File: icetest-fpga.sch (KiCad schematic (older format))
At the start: 25 parts

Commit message: add schematic notes
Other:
- note added: "CDONE pull up as per\nice40 handbook"
- note added: "RST high starts config process\nautomatically"
- note added: "SCLK pull up recommended\nby ice40 handbook"
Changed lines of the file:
@@
 	-1   0    0    1
 $EndComp
+Text Notes 6050 2600 0    60   ~ 0
+RST high starts config process\nautomatically
+Text Notes 8150 2900 0    60   ~ 0
+CDONE pull up as per\nice40 handbook
+Text Notes 9100 1250 0    60   ~ 0
+SCLK pull up recommended\nby ice40 handbook
 $EndSCHEMATC

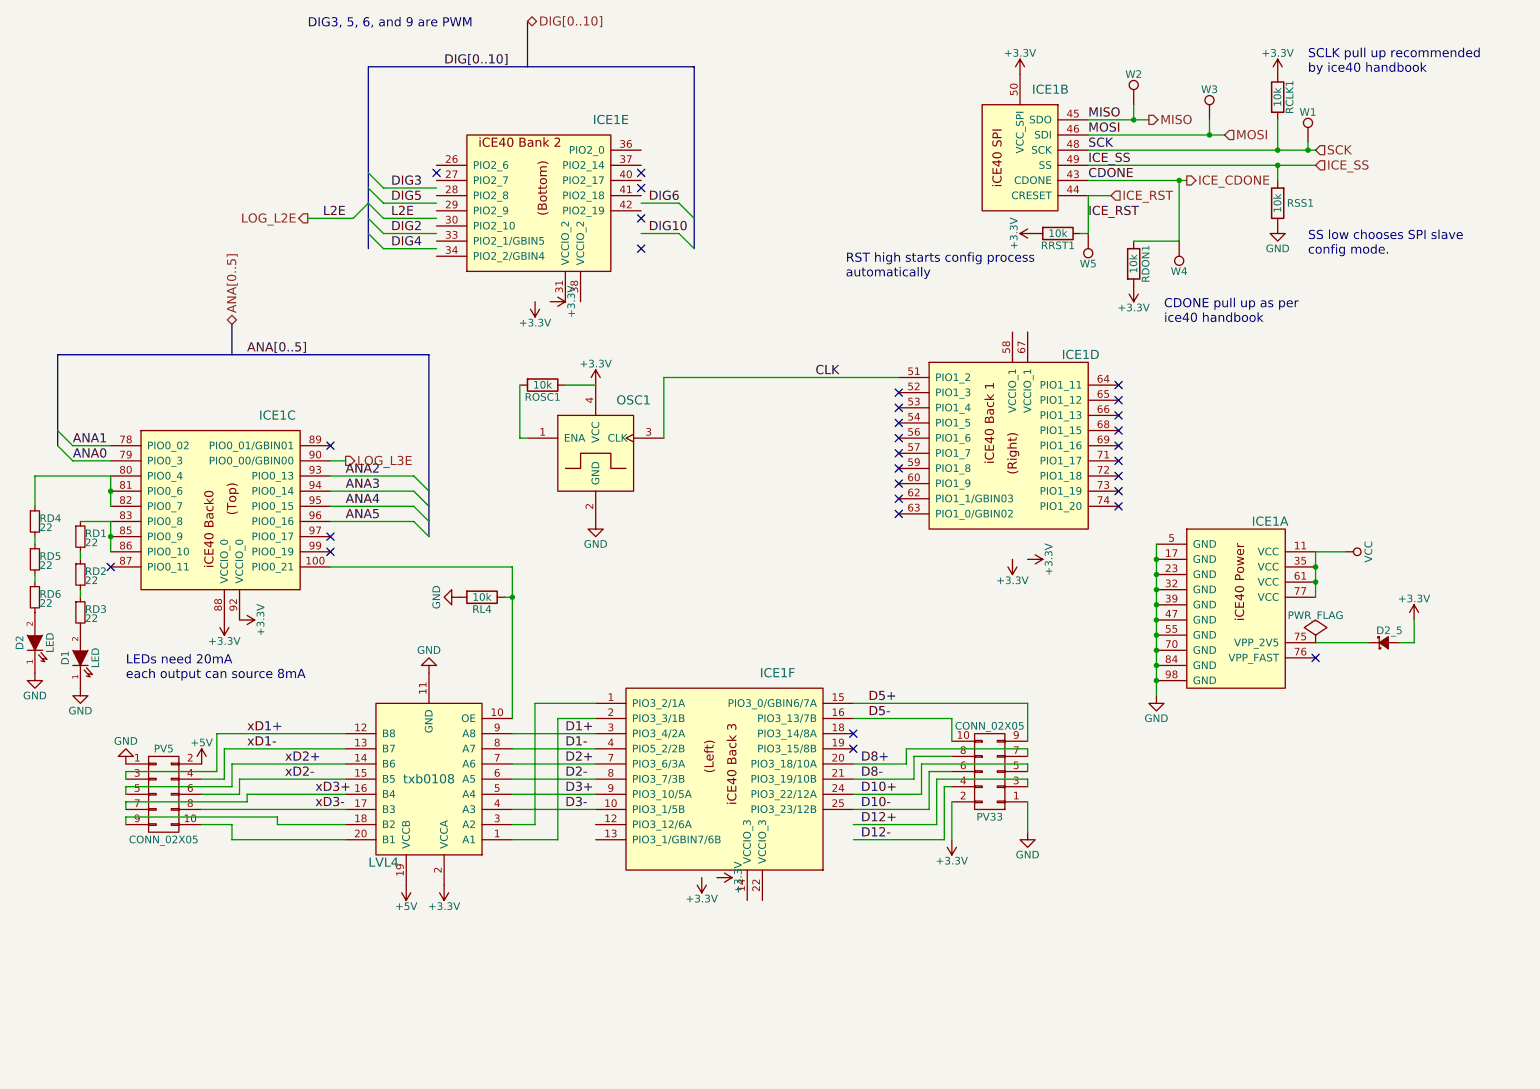
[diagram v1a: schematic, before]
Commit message: switch level shifter
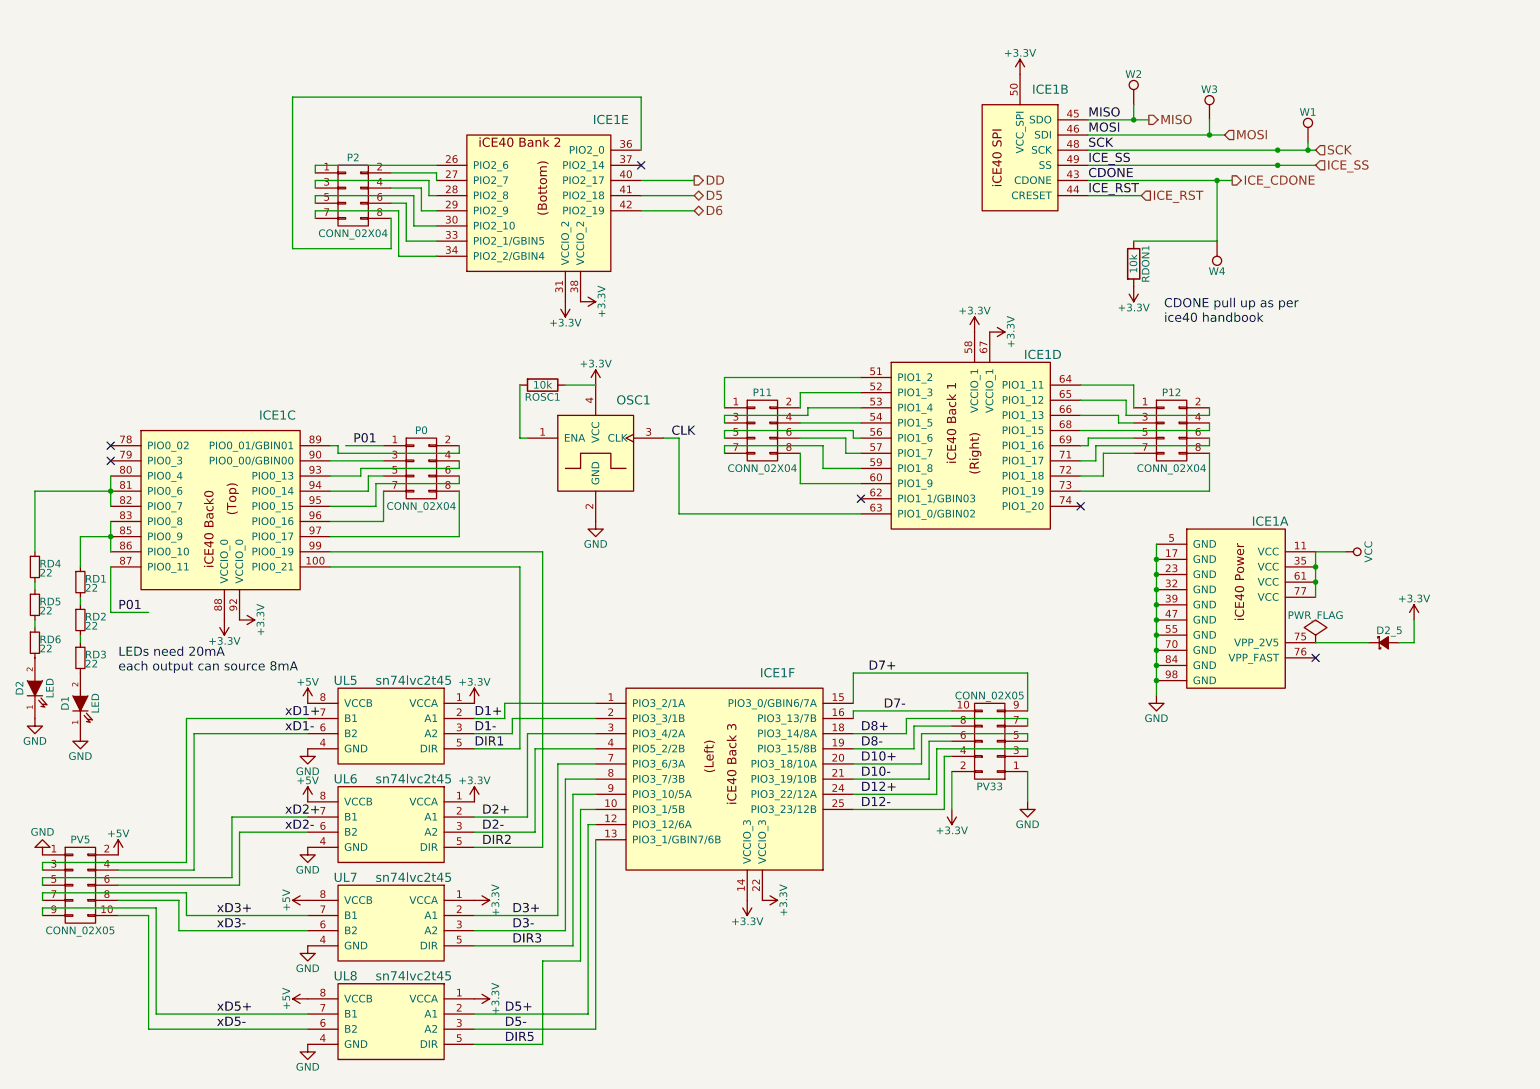
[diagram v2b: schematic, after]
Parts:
- removed LVL4: txb0108, local:PSO_20, symbol txb0108
- removed RCLK1, RL4, RRST1, RSS1: 10k, Resistors_SMD:R_0603_HandSoldering, symbol R
- removed W5: RST, Connect:PINTST, symbol TEST_1P
- added P0, P11, P12, P2: CONN_02X04, symbol CONN_02X04
- added UL5, UL6, UL7, UL8: sn74lvc2t45, symbol sn74lvc2t45
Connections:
- net labels added: D5, D6, D7+, D7-, DD, DIR1, DIR2, DIR3, DIR5, P01, xD5+, xD5-
- net labels removed: ANA0, ANA1, ANA2, ANA3, ANA4, ANA5, ANA[0..5], DIG10, DIG2, DIG3, DIG4, DIG5, DIG6, DIG[0..10], L2E, LOG_L2E, LOG_L3E
- wire segments 118 -> 224
- no-connect marks 30 -> 6
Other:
- note removed: "DIG3, 5, 6, and 9 are PWM"
- note removed: "RST high starts config process\nautomatically"
- note removed: "SCLK pull up recommended\nby ice40 handbook"
- note removed: "SS low chooses SPI slave\nconfig mode."
- moved on the sheet: D1, D2, ICE1D, PV33, PV5, RD1, RD2, RD3, RD4, RD5, RD6, W4

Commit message: redo layout
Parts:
- added W5: RST, Connect:PINTST, symbol TEST_1P
- P0, P11, P12, P2: footprint (none) -> Pin_Headers:Pin_Header_Straight_2x05; symbol CONN_02X04 -> CONN_02X05
- UL5, UL6, UL7, UL8: footprint (none) -> local:VSSOP-8
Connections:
- net +3V3: now also P0.1 (P1), P11.1 (P1), P12.1 (P1), P2.1 (P1)
- net D1+: now also UL5.3 (A2); no longer UL5.2 (A1)
- net D1-: now also UL5.2 (A1); no longer UL5.3 (A2)
- net D2+: now also UL6.3 (A2); no longer UL6.2 (A1)
- net D2-: now also UL6.2 (A1); no longer UL6.3 (A2)
- net D3+: now also UL7.3 (A2); no longer UL7.2 (A1)
- net D3-: now also UL7.2 (A1); no longer UL7.3 (A2)
- net D5+: now also UL8.3 (A2); no longer UL8.2 (A1)
- net D5-: now also UL8.2 (A1); no longer UL8.3 (A2)
- net GND: now also P0.2 (P2), P11.2 (P2), P12.2 (P2), P2.2 (P2)
- net ICE_RST: now also W5.1
- net P01: now also P0.3 (P3); no longer P0.1 (P1)
- net xD1+: now also UL5.6 (B2); no longer UL5.7 (B1)
- net xD1-: now also UL5.7 (B1); no longer UL5.6 (B2)
- net xD2+: now also UL6.6 (B2); no longer UL6.7 (B1)
- net xD2-: now also UL6.7 (B1); no longer UL6.6 (B2)
- net xD3+: now also UL7.6 (B2); no longer UL7.7 (B1)
- net xD3-: now also UL7.7 (B1); no longer UL7.6 (B2)
- net xD5+: now also UL8.6 (B2); no longer UL8.7 (B1)
- net xD5-: now also UL8.7 (B1); no longer UL8.6 (B2)
- net at ICE1.26 (PIO2_6): now also P2.4 (P4); no longer P2.1 (P1)
- net at ICE1.27 (PIO2_7): now also P2.3 (P3); no longer P2.2 (P2)
- net at ICE1.28 (PIO2_8): now also P2.6 (P6); no longer P2.3 (P3)
- net at ICE1.29 (PIO2_9): now also P2.5 (P5); no longer P2.4 (P4)
- net at ICE1.30 (PIO2_10): now also P2.8 (P8); no longer P2.5 (P5)
- net at ICE1.33 (PIO2_1/GBIN5): now also P2.7 (P7); no longer P2.6 (P6)
- net at ICE1.34 (PIO2_2/GBIN4): now also P2.10 (P10); no longer P2.7 (P7)
- net at ICE1.36 (PIO2_0): now also P2.9 (P9); no longer P2.8 (P8)
- net at ICE1.89 (PIO0_01/GBIN01): now also P0.4 (P4); no longer P0.2 (P2)
- net at ICE1.90 (PIO0_00/GBIN00): now also P0.5 (P5); no longer P0.3 (P3)
- net at ICE1.93 (PIO0_13): now also P0.6 (P6); no longer P0.4 (P4)
- net at ICE1.94 (PIO0_14): now also P0.7 (P7); no longer P0.5 (P5)
- net at ICE1.95 (PIO0_15): now also P0.8 (P8); no longer P0.6 (P6)
- net at ICE1.96 (PIO0_16): now also P0.9 (P9); no longer P0.7 (P7)
- net at ICE1.97 (PIO0_17): now also P0.10 (P10); no longer P0.8 (P8)
- net at ICE1.51 (PIO1_2): now also P11.4 (P4); no longer P11.1 (P1)
- net at ICE1.52 (PIO1_3): now also P11.3 (P3); no longer P11.2 (P2)
- net at ICE1.53 (PIO1_4): now also P11.6 (P6); no longer P11.3 (P3)
- net at ICE1.54 (PIO1_5): now also P11.5 (P5); no longer P11.4 (P4)
- net at ICE1.56 (PIO1_6): now also P11.8 (P8); no longer P11.5 (P5)
- net at ICE1.57 (PIO1_7): now also P11.7 (P7); no longer P11.6 (P6)
- net at ICE1.59 (PIO1_8): now also P11.10 (P10); no longer P11.7 (P7)
- net at ICE1.60 (PIO1_9): now also P11.9 (P9); no longer P11.8 (P8)
- net at ICE1.64 (PIO1_11): now also P12.3 (P3); no longer P12.1 (P1)
- net at ICE1.65 (PIO1_12): now also P12.4 (P4); no longer P12.2 (P2)
- net at ICE1.66 (PIO1_13): now also P12.5 (P5); no longer P12.3 (P3)
- net at ICE1.68 (PIO1_15): now also P12.6 (P6); no longer P12.4 (P4)
- net at ICE1.69 (PIO1_16): now also P12.7 (P7); no longer P12.5 (P5)
- net at ICE1.71 (PIO1_17): now also P12.8 (P8); no longer P12.6 (P6)
- net at ICE1.72 (PIO1_18): now also P12.9 (P9); no longer P12.7 (P7)
- net at ICE1.73 (PIO1_19): now also P12.10 (P10); no longer P12.8 (P8)

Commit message: more layout
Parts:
- added W6: SS, Connect:PINTST, symbol TEST_1P
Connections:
- net ICE_SS: now also W6.1
- net D5+ renamed D6+
- net D5- renamed D6-
- net DIR5 renamed DIR6
- net xD5+ renamed xD6+
- net xD5- renamed xD6-

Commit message: more layout
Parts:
- added RDR1, RDR2, RDR3, RDR6: 10k, Resistors_SMD:R_0603_HandSoldering, symbol R
- added W7: CLK, Measurement_Points:Measurement_Point_Square-SMD-Pad_Small, symbol TEST_1P
- P0, P11, P12, P2: value CONN_02X04 -> CONN_02X05
- W1, W2, W3, W4, W5, W6: footprint Connect:PINTST -> Measurement_Points:Measurement_Point_Square-SMD-Pad_Small
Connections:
- net CLK: now also W7.1
- net DIR1: now also RDR1.1
- net DIR2: now also RDR2.1
- net DIR3: now also RDR3.1
- net DIR6: now also RDR6.1
- net GND: now also RDR1.2, RDR2.2, RDR3.2, RDR6.2
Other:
- note added: "pull-down to stabalize direction during\npowerup/configuration"
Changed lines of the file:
@@
 Text HLabel 9150 1850 2    60   Input ~ 0
 ICE_SS
-Text HLabel 8600 1950 2    60   Output ~ 0
+Text HLabel 8700 2350 2    60   Output ~ 0
 ICE_CDONE
 Text HLabel 8000 2050 2    60   Input ~ 0
@@
 F 0 "W1" H 9100 1900 50  0000 C CNN
 F 1 "SCLK" H 9100 1900 50  0001 C CNN
-F 2 "Connect:PINTST" H 9300 1700 50  0001 C CNN
+F 2 "Measurement_Points:Measurement_Point_Square-SMD-Pad_Small" H 9300 1700 50  0001 C CNN
 F 3 "" H 9300 1700 50  0000 C CNN
 	1    9100 1700
@@
 F 0 "W2" H 7950 1650 50  0000 C CNN
 F 1 "MISO" H 7950 1650 50  0001 C CNN
-F 2 "Connect:PINTST" H 8150 1450 50  0001 C CNN
+F 2 "Measurement_Points:Measurement_Point_Square-SMD-Pad_Small" H 8150 1450 50  0001 C CNN
 F 3 "" H 8150 1450 50  0000 C CNN
 	1    7950 1450
@@
 F 0 "W3" H 8450 1750 50  0000 C CNN
 F 1 "MOSI" H 8450 1750 50  0001 C CNN
-F 2 "Connect:PINTST" H 8650 1550 50  0001 C CNN
+F 2 "Measurement_Points:Measurement_Point_Square-SMD-Pad_Small" H 8650 1550 50  0001 C CNN
 F 3 "" H 8650 1550 50  0000 C CNN
 	1    8450 1550
@@
 F 0 "W4" H 8500 2550 50  0000 C CNN
 F 1 "CDONE" H 8500 2550 50  0001 C CNN
-F 2 "Connect:PINTST" H 8700 2350 50  0001 C CNN
+F 2 "Measurement_Points:Measurement_Point_Square-SMD-Pad_Small" H 8700 2350 50  0001 C CNN
 F 3 "" H 8700 2350 50  0000 C CNN
 	1    8500 2350
@@
 P 3250 3800
 F 0 "P0" H 3250 4100 50  0000 C CNN
-F 1 "CONN_02X04" H 3250 3550 50  0000 C CNN
+F 1 "CONN_02X05" H 3250 3550 50  0000 C CNN
 F 2 "Pin_Headers:Pin_Header_Straight_2x05" H 3250 2600 50  0001 C CNN
 F 3 "" H 3250 2600 50  0000 C CNN
@@
 P 2800 2000
 F 0 "P2" H 2800 2300 50  0000 C CNN
-F 1 "CONN_02X04" H 2800 1750 50  0000 C CNN
+F 1 "CONN_02X05" H 2800 1750 50  0000 C CNN
 F 2 "Pin_Headers:Pin_Header_Straight_2x05" H 2800 800 50  0001 C CNN
 F 3 "" H 2800 800 50  0000 C CNN
@@
 P 5500 3550
 F 0 "P11" H 5500 3900 50  0000 C CNN
-F 1 "CONN_02X04" H 5500 3300 50  0000 C CNN
+F 1 "CONN_02X05" H 5500 3300 50  0000 C CNN
 F 2 "Pin_Headers:Pin_Header_Straight_2x05" H 5500 2350 50  0001 C CNN
 F 3 "" H 5500 2350 50  0000 C CNN
@@
 P 8200 3550
 F 0 "P12" H 8200 3850 50  0000 C CNN
-F 1 "CONN_02X04" H 8200 3300 50  0000 C CNN
+F 1 "CONN_02X05" H 8200 3300 50  0000 C CNN
 F 2 "Pin_Headers:Pin_Header_Straight_2x05" H 8200 2350 50  0001 C CNN
 F 3 "" H 8200 2350 50  0000 C CNN
@@
 	7650 1850 9150 1850
 Wire Wire Line
-	7650 1950 8600 1950
-Wire Wire Line
-	8000 2050 7650 2050
+	7650 1950 8500 1950
+Wire Wire Line
+	7650 2050 8000 2050
 Wire Wire Line
 	8100 4350 8100 5350
@@
 	8500 1950 8500 2350
 Wire Wire Line
-	8500 2350 7950 2350
+	7950 2350 8700 2350
 Connection ~ 8500 1950
 Connection ~ 8900 1750
@@
 F 0 "W5" H 7700 2350 50  0000 C CNN
 F 1 "RST" H 7700 2350 50  0001 C CNN
-F 2 "Connect:PINTST" H 7900 2150 50  0001 C CNN
+F 2 "Measurement_Points:Measurement_Point_Square-SMD-Pad_Small" H 7900 2150 50  0001 C CNN
 F 3 "" H 7900 2150 50  0000 C CNN
 	1    7700 2150
@@
 F 0 "W6" H 8900 2050 50  0000 C CNN
 F 1 "SS" H 8900 2050 50  0001 C CNN
-F 2 "Connect:PINTST" H 9100 1850 50  0001 C CNN
+F 2 "Measurement_Points:Measurement_Point_Square-SMD-Pad_Small" H 9100 1850 50  0001 C CNN
 F 3 "" H 9100 1850 50  0000 C CNN
 	1    8900 1850
 	-1   0    0    1
 $EndComp
+Connection ~ 8500 2350
+$Comp
+L R RDR1
+U 1 1 58030EFC
+P 4750 4800
+F 0 "RDR1" V 4830 4800 50  0000 C CNN
+F 1 "10k" V 4750 4800 50  0000 C CNN
+F 2 "Resistors_SMD:R_0603_HandSoldering" V 4680 4800 50  0001 C CNN
+F 3 "" H 4750 4800 50  0000 C CNN
+	1    4750 4800
+	1    0    0    -1
+$EndComp
+$Comp
+L GND #PWR0114
+U 1 1 58031065
+P 4750 4950
+F 0 "#PWR0114" H 4750 4700 50  0001 C CNN
+F 1 "GND" H 4750 4800 50  0000 C CNN
+F 2 "" H 4750 4950 50  0000 C CNN
+F 3 "" H 4750 4950 50  0000 C CNN
+	1    4750 4950
+	1    0    0    -1
+$EndComp
+Wire Wire Line
+	4750 4650 4750 4500
+$Comp
+L R RDR2
+U 1 1 5803131B
+P 4950 4800
+F 0 "RDR2" V 5030 4800 50  0000 C CNN
+F 1 "10k" V 4950 4800 50  0000 C CNN
+F 2 "Resistors_SMD:R_0603_HandSoldering" V 4880 4800 50  0001 C CNN
+F 3 "" H 4950 4800 50  0000 C CNN
+	1    4950 4800
+	1    0    0    -1
+$EndComp
+$Comp
+L GND #PWR0115
+U 1 1 58031321
+P 4950 4950
+F 0 "#PWR0115" H 4950 4700 50  0001 C CNN
+F 1 "GND" H 4950 4800 50  0000 C CNN
+F 2 "" H 4950 4950 50  0000 C CNN
+F 3 "" H 4950 4950 50  0000 C CNN
+	1    4950 4950
+	1    0    0    -1
+$EndComp
+Wire Wire Line
+	4950 4650 4950 4500
+$Comp
+L R RDR3
+U 1 1 5803137C
+P 5150 4800
+F 0 "RDR3" V 5230 4800 50  0000 C CNN
+F 1 "10k" V 5150 4800 50  0000 C CNN
+F 2 "Resistors_SMD:R_0603_HandSoldering" V 5080 4800 50  0001 C CNN
+F 3 "" H 5150 4800 50  0000 C CNN
+	1    5150 4800
+	1    0    0    -1
+$EndComp
+$Comp
+L GND #PWR0116
+U 1 1 58031382
+P 5150 4950
+F 0 "#PWR0116" H 5150 4700 50  0001 C CNN
+F 1 "GND" H 5150 4800 50  0000 C CNN
+F 2 "" H 5150 4950 50  0000 C CNN
+F 3 "" H 5150 4950 50  0000 C CNN
+	1    5150 4950
+	1    0    0    -1
+$EndComp
+Wire Wire Line
+	5150 4650 5150 4500
+$Comp
+L R RDR6
+U 1 1 5803141A
+P 5350 4800
+F 0 "RDR6" V 5430 4800 50  0000 C CNN
+F 1 "10k" V 5350 4800 50  0000 C CNN
+F 2 "Resistors_SMD:R_0603_HandSoldering" V 5280 4800 50  0001 C CNN
+F 3 "" H 5350 4800 50  0000 C CNN
+	1    5350 4800
+	1    0    0    -1
+$EndComp
+$Comp
+L GND #PWR0117
+U 1 1 58031420
+P 5350 4950
+F 0 "#PWR0117" H 5350 4700 50  0001 C CNN
+F 1 "GND" H 5350 4800 50  0000 C CNN
+F 2 "" H 5350 4950 50  0000 C CNN
+F 3 "" H 5350 4950 50  0000 C CNN
+	1    5350 4950
+	1    0    0    -1
+$EndComp
+Wire Wire Line
+	5350 4650 5350 4500
+Text Label 4750 4600 1    60   ~ 0
+DIR1
+Text Label 4950 4600 1    60   ~ 0
+DIR2
+Text Label 5150 4600 1    60   ~ 0
+DIR3
+Text Label 5350 4600 1    60   ~ 0
+DIR6
+Text Notes 5500 4800 0    60   ~ 0
+pull-down to stabalize direction during\npowerup/configuration
+$Comp
+L TEST_1P W7
+U 1 1 58039B13
+P 5700 4200
+F 0 "W7" H 5700 4400 50  0000 C CNN
+F 1 "CLK" H 5600 4350 50  0000 C CNN
+F 2 "Measurement_Points:Measurement_Point_Square-SMD-Pad_Small" H 5900 4200 50  0001 C CNN
+F 3 "" H 5900 4200 50  0000 C CNN
+	1    5700 4200
+	-1   0    0    1
+$EndComp
+Wire Wire Line
+	5700 4200 5700 4150
+Connection ~ 5700 4150
 $EndSCHEMATC
